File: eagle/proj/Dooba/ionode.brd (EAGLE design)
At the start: 43.2 x 15.2 mm, 34 parts, among them J2 USB-BAMPHENOL-MICRO, U1 ATMEGA1284P-MU44-VQFN, U4 FT232RQFN32, U5 SN74LVC1G125SOT23-5, U6 SN74LVC1G125SOT23-5, U7 3.3V, X1 10MHz

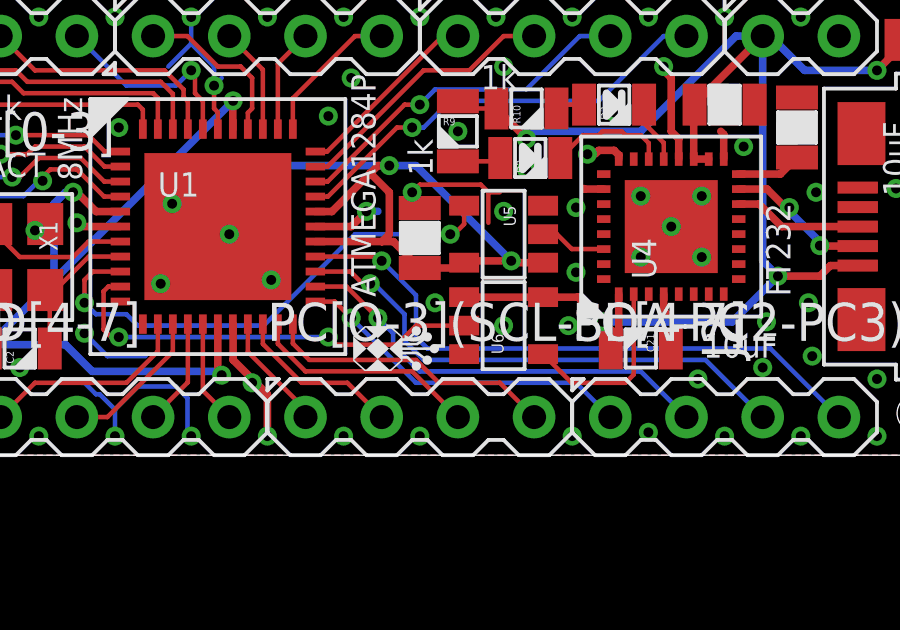
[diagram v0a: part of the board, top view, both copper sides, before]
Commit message: Fixed STA013 Device in Eagle Library Fixed Aecho Board to use updated STA013 Fixed ioNode Schematic (74125 buffers for USB UART had their !OE tied to VCC...)
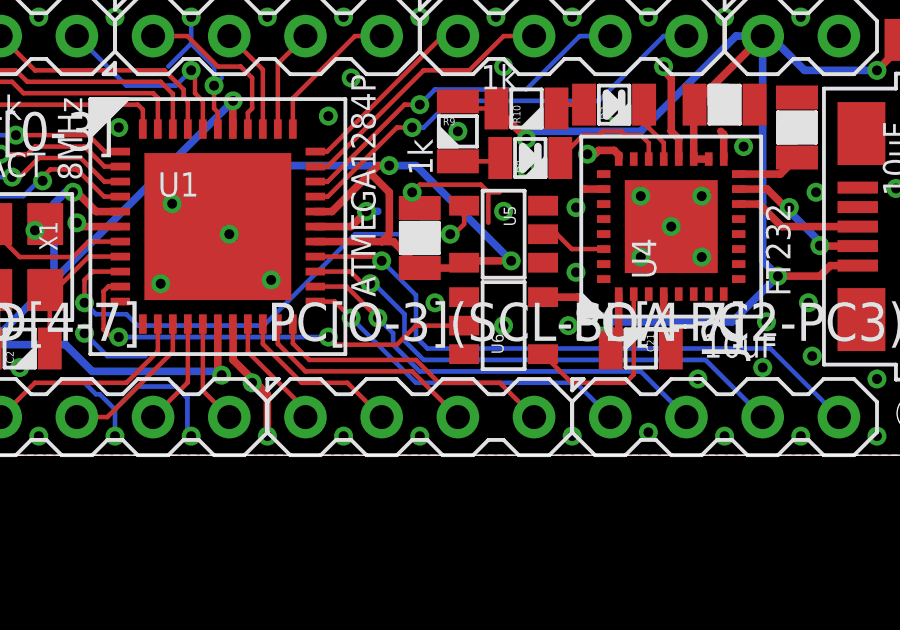
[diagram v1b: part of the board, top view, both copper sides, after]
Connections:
- net 3.3V: no longer U5.1
- net GND: now also U5.1, U6.1
- net VUSB: no longer U6.1
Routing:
- net VUSB: track 48.6 -> 46.0 mm
- net 3.3V: track 63.3 -> 62.3 mm
